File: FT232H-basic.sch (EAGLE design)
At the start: 26 parts, among them IC1 FT232H

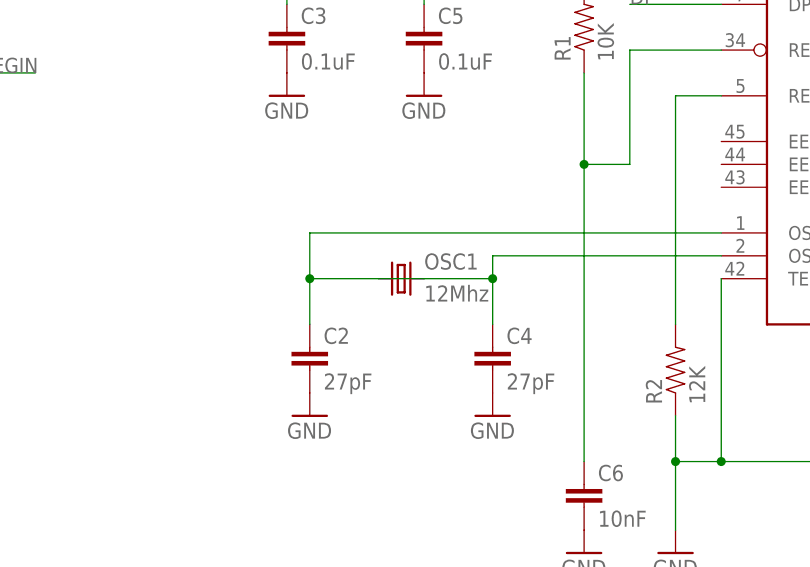
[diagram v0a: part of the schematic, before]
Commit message: routing improvements - much simpler, has bottom ground plane and top copper pour
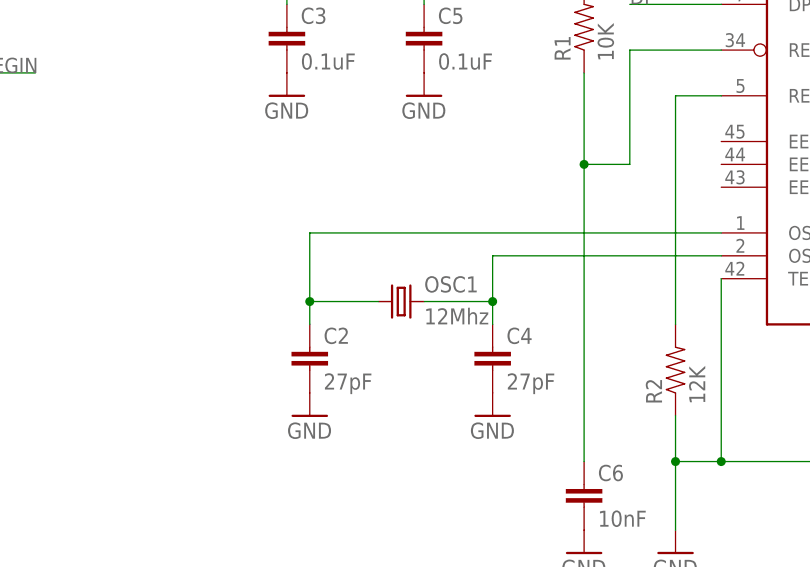
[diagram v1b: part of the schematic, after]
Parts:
- D1: device SparkFun-LED:LED-GREENLARGE -> SparkFun-LED:LED-GREEN0603
- OSC1: device SparkFun-FreqCtrl:CRYSTALHC49US -> SparkFun-FreqCtrl:CRYSTAL5X3
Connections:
- new net N$7: C4.1, IC1.OSCO, OSC1.2
- net OSC1: no longer C4.1, IC1.OSCO, OSC1.2
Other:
- moved on the sheet: OSC1
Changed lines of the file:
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@@
 <part name="GND1" library="SparkFun-Aesthetics" deviceset="GND" device=""/>
 <part name="GND2" library="SparkFun-Aesthetics" deviceset="GND" device=""/>
-<part name="OSC1" library="SparkFun-FreqCtrl" deviceset="CRYSTAL" device="HC49US" value="12Mhz"/>
 <part name="C2" library="SparkFun-Capacitors" deviceset="0.1UF-25V-5%(0603)" device="" value="27pF"/>
 <part name="C4" library="SparkFun-Capacitors" deviceset="0.1UF-25V-5%(0603)" device="" value="27pF"/>
@@
 <part name="GND11" library="SparkFun-Aesthetics" deviceset="GND" device=""/>
 <part name="R3" library="SparkFun-Resistors" deviceset="1K-1%" device="" value="1k"/>
-<part name="D1" library="SparkFun-LED" deviceset="LED-GREEN" device="LARGE" value="GREEN"/>
 <part name="GND12" library="SparkFun-Aesthetics" deviceset="GND" device=""/>
 <part name="C1" library="SparkFun-Capacitors" deviceset="0.1UF-25V-5%(0603)" device="" value="0.1uF"/>
@@
 <part name="GND16" library="SparkFun-Aesthetics" deviceset="GND" device=""/>
 <part name="GND17" library="SparkFun-Aesthetics" deviceset="GND" device=""/>
+<part name="D1" library="SparkFun-LED" deviceset="LED-GREEN" device="0603" value="GREEN"/>
+<part name="OSC1" library="SparkFun-FreqCtrl" deviceset="CRYSTAL" device="5X3" value="12Mhz"/>
 <part name="FRAME1" library="SparkFun-Aesthetics" deviceset="FRAME-LETTER" device=""/>
 </parts>
@@
 <instance part="GND1" gate="1" x="86.36" y="88.9"/>
 <instance part="GND2" gate="1" x="101.6" y="88.9"/>
-<instance part="OSC1" gate="G$1" x="99.06" y="68.58"/>
 <instance part="C2" gate="G$1" x="88.9" y="58.42"/>
 <instance part="C4" gate="G$1" x="109.22" y="58.42"/>
@@
 <instance part="GND11" gate="1" x="180.34" y="129.54"/>
 <instance part="R3" gate="G$1" x="172.72" y="162.56"/>
-<instance part="D1" gate="G$1" x="180.34" y="162.56" rot="R90"/>
 <instance part="GND12" gate="1" x="190.5" y="160.02"/>
 <instance part="C1" gate="G$1" x="35.56" y="83.82"/>
@@
 <instance part="GND16" gate="1" x="220.98" y="50.8"/>
 <instance part="GND17" gate="1" x="236.22" y="50.8"/>
+<instance part="D1" gate="G$1" x="180.34" y="162.56" rot="R90"/>
+<instance part="OSC1" gate="G$1" x="99.06" y="66.04"/>
 <instance part="FRAME1" gate="G$1" x="0" y="0"/>
 <instance part="FRAME1" gate="G$2" x="147.32" y="0"/>
@@
 </segment>
 <segment>
-<pinref part="D1" gate="G$1" pin="C"/>
 <pinref part="GND12" gate="1" pin="GND"/>
 <wire x1="185.42" y1="162.56" x2="190.5" y2="162.56" width="0.1524" layer="91"/>
+<pinref part="D1" gate="G$1" pin="C"/>
 </segment>
 <segment>
@@
 <pinref part="C2" gate="G$1" pin="1"/>
 <wire x1="134.62" y1="73.66" x2="88.9" y2="73.66" width="0.1524" layer="91"/>
-<wire x1="88.9" y1="73.66" x2="88.9" y2="68.58" width="0.1524" layer="91"/>
+<wire x1="88.9" y1="73.66" x2="88.9" y2="66.04" width="0.1524" layer="91"/>
+<wire x1="88.9" y1="66.04" x2="88.9" y2="63.5" width="0.1524" layer="91"/>
+<wire x1="96.52" y1="66.04" x2="88.9" y2="66.04" width="0.1524" layer="91"/>
+<junction x="88.9" y="66.04"/>
 <pinref part="OSC1" gate="G$1" pin="1"/>
-<wire x1="88.9" y1="68.58" x2="88.9" y2="63.5" width="0.1524" layer="91"/>
-<wire x1="88.9" y1="68.58" x2="96.52" y2="68.58" width="0.1524" layer="91"/>
-<pinref part="OSC1" gate="G$1" pin="2"/>
-<wire x1="96.52" y1="68.58" x2="101.6" y2="68.58" width="0.1524" layer="91"/>
-<pinref part="IC1" gate="G$1" pin="OSCO"/>
-<pinref part="C4" gate="G$1" pin="1"/>
-<wire x1="134.62" y1="71.12" x2="109.22" y2="71.12" width="0.1524" layer="91"/>
-<wire x1="109.22" y1="71.12" x2="109.22" y2="68.58" width="0.1524" layer="91"/>
-<wire x1="109.22" y1="68.58" x2="109.22" y2="63.5" width="0.1524" layer="91"/>
-<wire x1="101.6" y1="68.58" x2="109.22" y2="68.58" width="0.1524" layer="91"/>
-<junction x="88.9" y="68.58"/>
-<junction x="109.22" y="68.58"/>
 </segment>
 </net>
@@
 <wire x1="124.46" y1="81.28" x2="119.38" y2="81.28" width="0.1524" layer="91"/>
 <junction x="119.38" y="81.28"/>
-</segment>
-</net>
-<net name="N$7" class="0">
-<segment>
-<pinref part="R3" gate="G$1" pin="2"/>
-<pinref part="D1" gate="G$1" pin="A"/>
 </segment>
 </net>
@@
 </segment>
 </net>
+<net name="N$5" class="0">
+<segment>
+<pinref part="R3" gate="G$1" pin="2"/>
+<pinref part="D1" gate="G$1" pin="A"/>
+</segment>
+</net>
+<net name="N$7" class="0">
+<segment>
+<pinref part="C4" gate="G$1" pin="1"/>
+<pinref part="IC1" gate="G$1" pin="OSCO"/>
+<wire x1="134.62" y1="71.12" x2="109.22" y2="71.12" width="0.1524" layer="91"/>
+<wire x1="109.22" y1="71.12" x2="109.22" y2="66.04" width="0.1524" layer="91"/>
+<wire x1="109.22" y1="66.04" x2="109.22" y2="63.5" width="0.1524" layer="91"/>
+<wire x1="101.6" y1="66.04" x2="109.22" y2="66.04" width="0.1524" layer="91"/>
+<junction x="109.22" y="66.04"/>
+<pinref part="OSC1" gate="G$1" pin="2"/>
+</segment>
+</net>

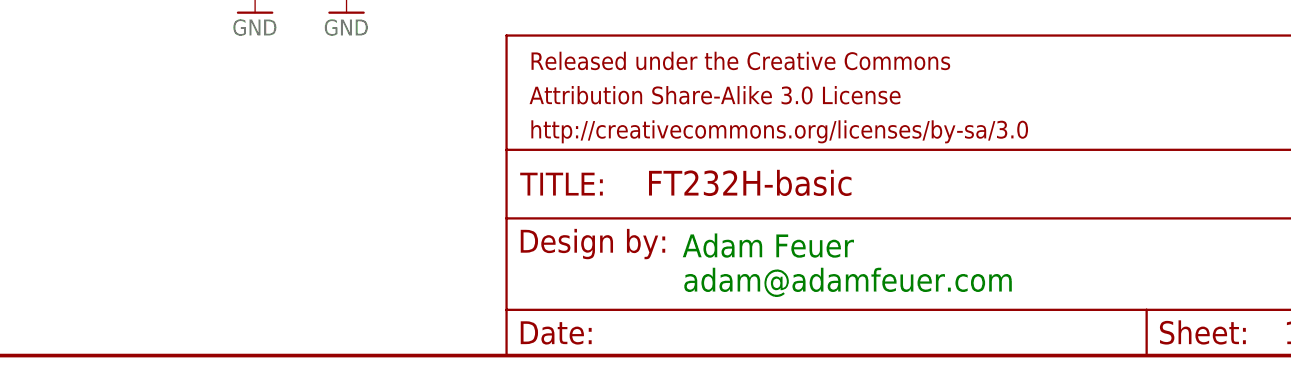
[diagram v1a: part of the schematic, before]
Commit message: board routed, passes DRC, and has silkscreen; not all fonts are vector
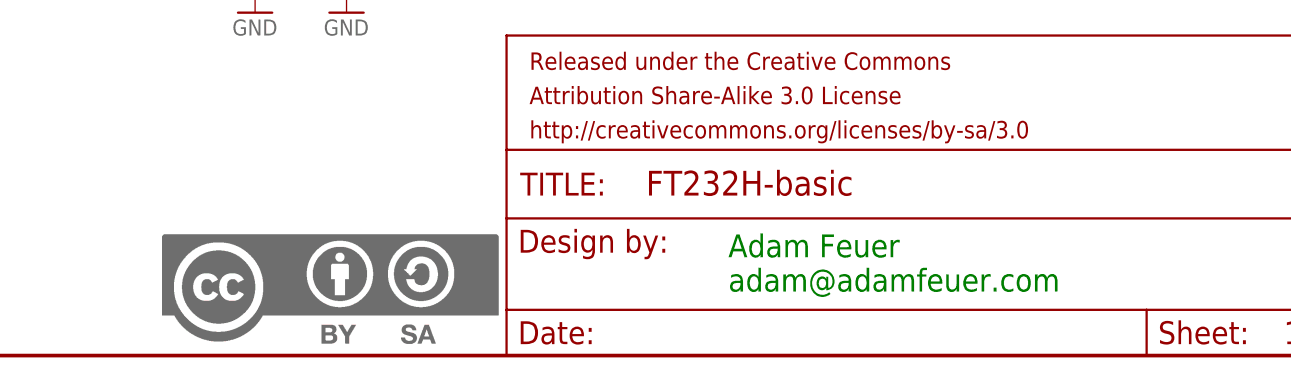
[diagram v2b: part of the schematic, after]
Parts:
- added U$2: CC-BY-SA, creative-commons:CC-BY-SA
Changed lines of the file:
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@@
 <layer number="151" name="HeatSink" color="7" fill="1" visible="no" active="yes"/>
 <layer number="199" name="Contour" color="7" fill="1" visible="no" active="yes"/>
-<layer number="200" name="200bmp" color="1" fill="10" visible="no" active="yes"/>
+<layer number="200" name="200bmp" color="1" fill="10" visible="yes" active="yes"/>
 <layer number="201" name="201bmp" color="2" fill="10" visible="no" active="yes"/>
 <layer number="202" name="202bmp" color="3" fill="10" visible="no" active="yes"/>
@@
 <part name="OSC1" library="SparkFun-FreqCtrl" deviceset="CRYSTAL" device="5X3" value="12Mhz"/>
 <part name="FRAME1" library="SparkFun-Aesthetics" deviceset="FRAME-LETTER" device=""/>
+<part name="U$2" library="creative-commons" deviceset="CC-BY-SA" device=""/>
 </parts>
 <sheets>
 <sheet>
 <plain>
-<text x="166.878" y="7.112" size="2.54" layer="91">Adam Feuer
+<text x="171.958" y="7.112" size="2.54" layer="91">Adam Feuer
 adam@adamfeuer.com</text>
 <text x="239.014" y="7.112" size="2.54" layer="91">0.1</text>
@@
 <instance part="FRAME1" gate="G$1" x="0" y="0"/>
 <instance part="FRAME1" gate="G$2" x="147.32" y="0"/>
+<instance part="U$2" gate="G$1" x="108.712" y="0.508"/>
 </instances>
 <busses>
